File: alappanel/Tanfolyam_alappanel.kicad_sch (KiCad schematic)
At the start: 35 parts, among them J1 Connector, J2 Connector, J3 Connector, SW1 SW_Push, SW2 SW_Push, U1 74HC595, U2 74HC595, U3 SA39-11SRWA, U4 SA39-11SRWA

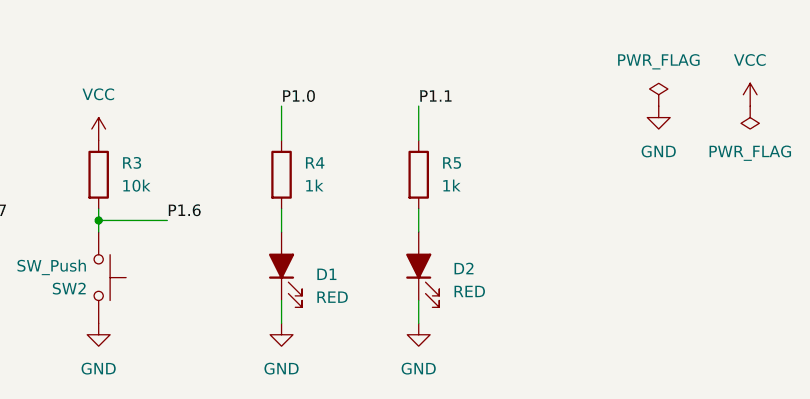
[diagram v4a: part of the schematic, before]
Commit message: Interaktív BOM, már a FAB rétegek feliratai is jó helyen vannak
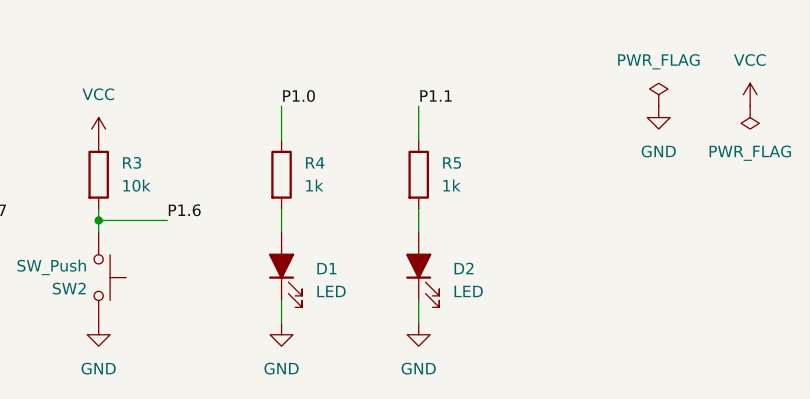
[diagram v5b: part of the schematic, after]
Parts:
- D1, D2: value RED -> LED
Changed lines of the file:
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@@
 			)
 		)
-		(property "Value" "RED"
+		(property "Value" "LED"
 			(at 140.97 171.7674 90)
 			(effects
@@
 		(fields_autoplaced yes)
 		(property "Reference" "D1"
-			(at 125.73 169.8625 90)
+			(at 125.73 169.2274 90)
 			(effects
 				(font
@@
 			)
 		)
-		(property "Value" "RED"
-			(at 125.73 172.4025 90)
-			(effects
-				(font
+		(property "Value" "LED"
+			(at 125.73 171.7674 90)
+			(effects
+				(font
